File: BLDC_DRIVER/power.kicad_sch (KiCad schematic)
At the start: 0 parts

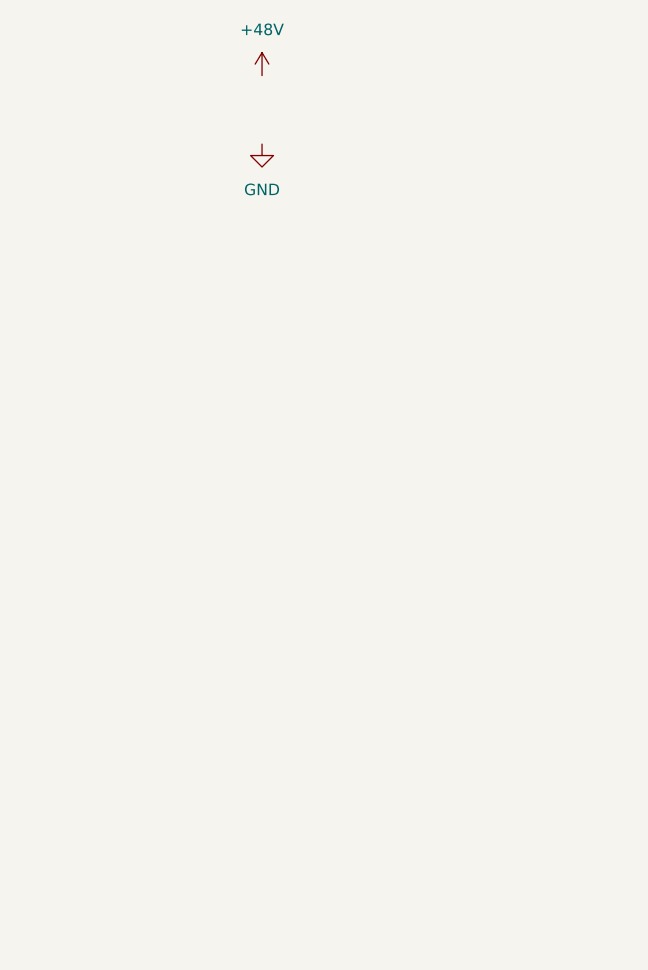
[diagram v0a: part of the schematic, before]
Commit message: buck and mcu added
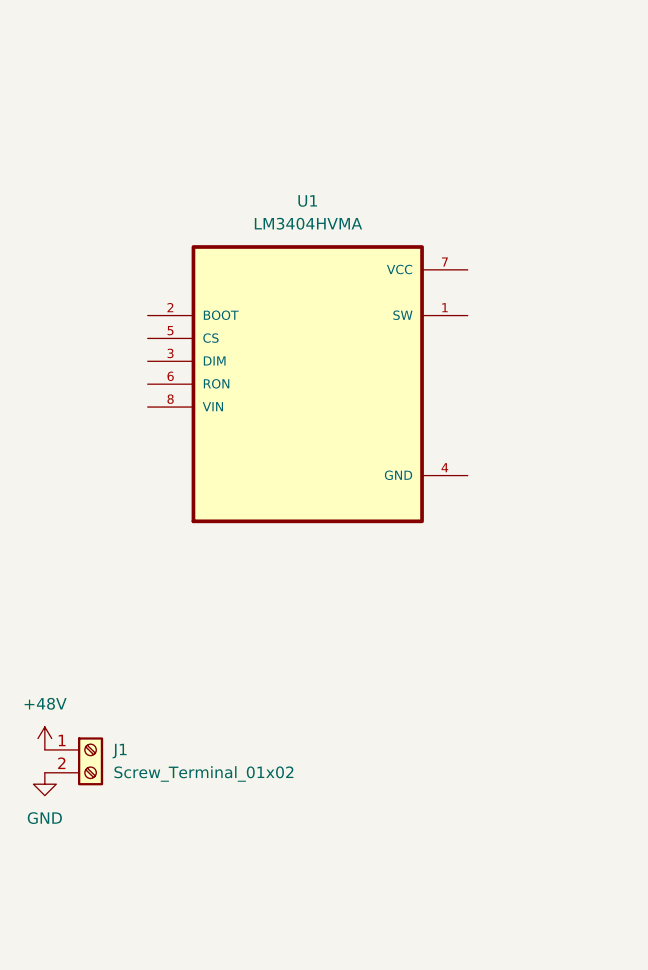
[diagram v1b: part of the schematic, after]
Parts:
- added J1: Screw_Terminal_01x02, TerminalBlock:TerminalBlock_MaiXu_MX126-5.0-02P_1x02_P5.00mm, symbol Connector:Screw_Terminal_01x02
- added U1: LM3404HVMA, LM3404:SOIC127P599X175-8N, symbol LM3404:LM3404HVMA
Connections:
- net +48V: now also J1.1 (Pin_1)
- net GND: now also J1.2 (Pin_2)

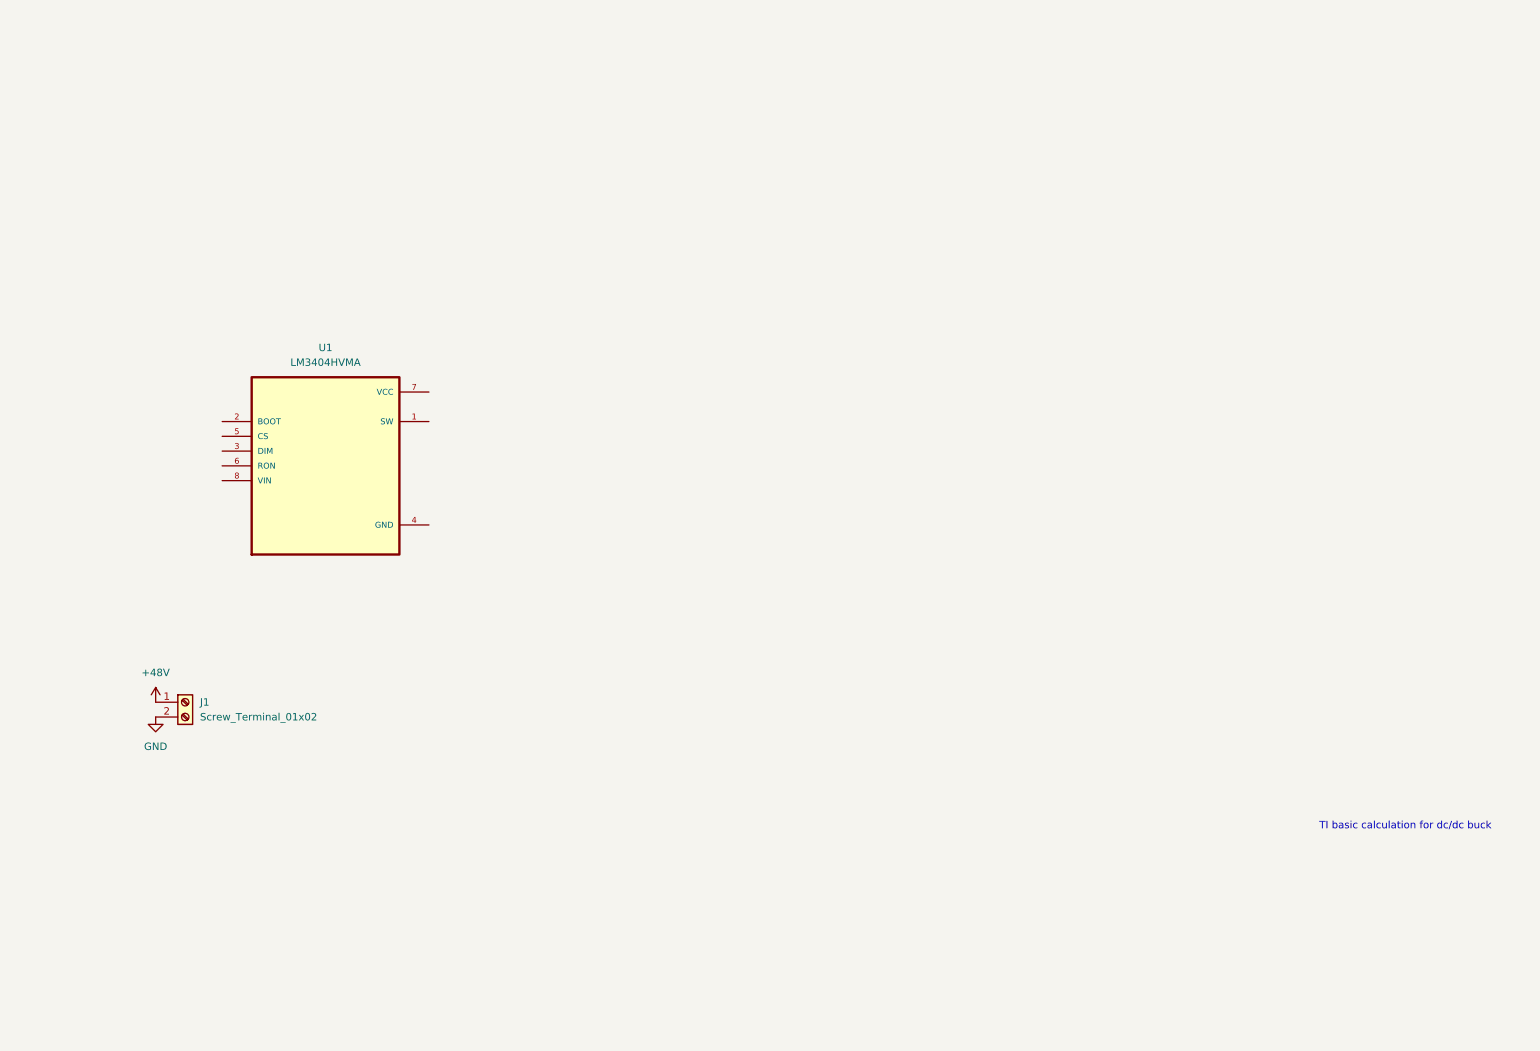
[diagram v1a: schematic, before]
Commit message: ldo added
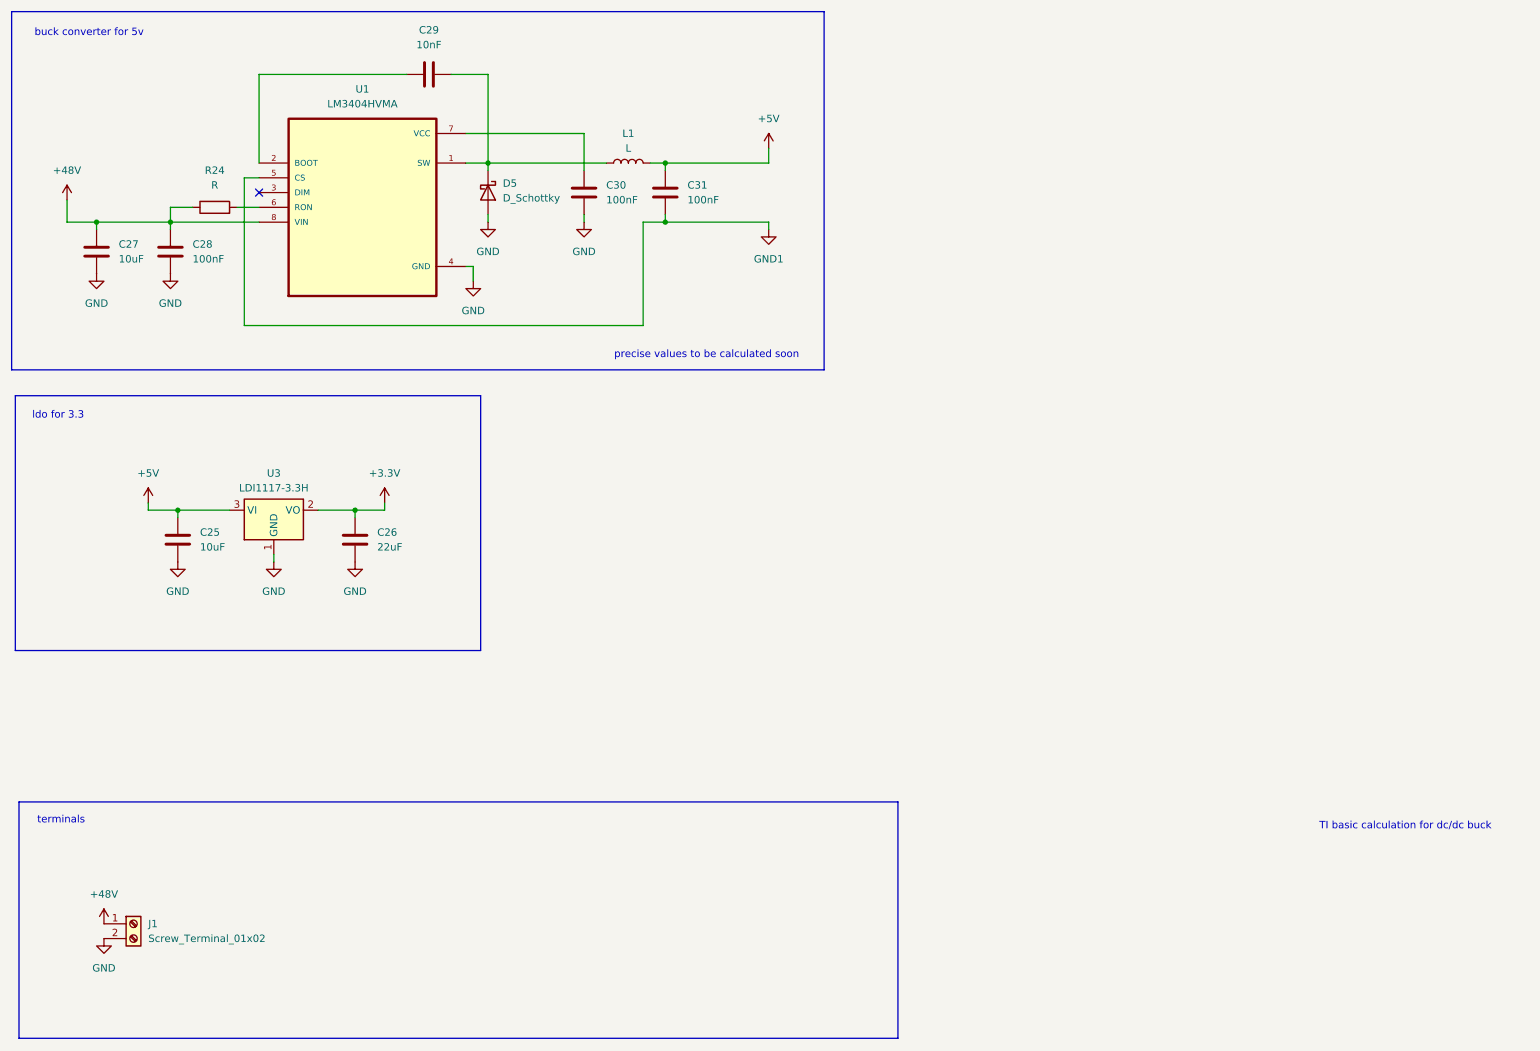
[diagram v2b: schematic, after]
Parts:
- added C25, C27: 10uF, symbol Device:C
- added C26: 22uF, symbol Device:C
- added C28, C30, C31: 100nF, symbol Device:C
- added C29: 10nF, symbol Device:C
- added D5: D_Schottky, symbol Device:D_Schottky
- added L1: L, symbol Device:L
- added R24: R, symbol Device:R
- added U3: LDI1117-3.3H, Package_TO_SOT_SMD:SOT-223-3_TabPin2, symbol Regulator_Linear:LM1117MP-3.3
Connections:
- net +48V: now also U1.8 (VIN), C27.1, C28.2, R24.1
- net GND: now also U1.4 (GND), C25.2, C26.2, C27.2, C28.1, C30.2, D5.2 (A), U3.1 (GND)
- net at U1.1 (SW): now also C29.2, D5.1 (K), L1.1
- net at U1.2 (BOOT): now also C29.1
- net GND1: now reaches U1.5 (CS)
- net GND1: now also C31.1
- net at U1.6 (RON): now also R24.2
- net at U1.7 (VCC): now also C30.1
- new net +3.3V: C26.1, U3.2 (VO)
- new net +5V: C25.1, C31.2, L1.2, U3.3 (VI)
- no-connect marks 0 -> 1
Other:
- note added: "buck converter for 5v"
- note added: "ldo for 3.3"
- note added: "precise values to be calculated soon"
- note added: "terminals"
- moved on the sheet: J1, U1

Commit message: mcu added
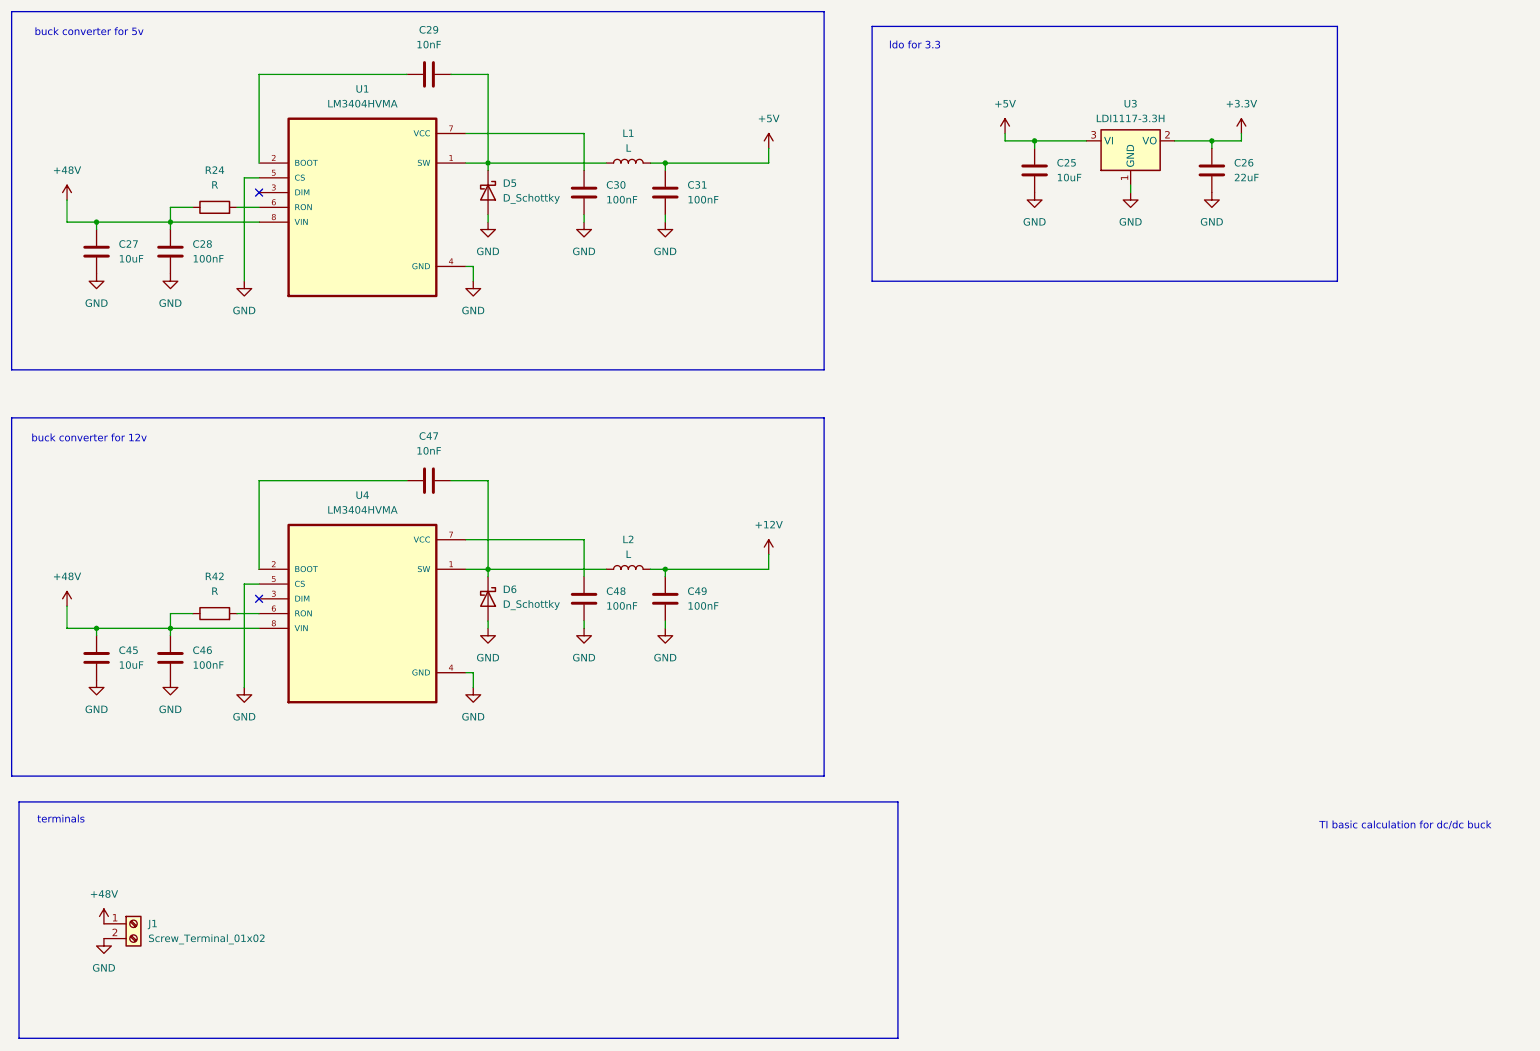
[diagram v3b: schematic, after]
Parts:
- added C45: 10uF, symbol Device:C
- added C46, C48, C49: 100nF, symbol Device:C
- added C47: 10nF, symbol Device:C
- added D6: D_Schottky, symbol Device:D_Schottky
- added L2: L, symbol Device:L
- added R42: R, symbol Device:R
- added U4: LM3404HVMA, LM3404:SOIC127P599X175-8N, symbol LM3404:LM3404HVMA
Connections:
- net GND1 is gone; now on net GND: C31.1, U1.5 (CS)
- net +48V: now also C45.1, C46.2, R42.1, U4.8 (VIN)
- net GND: now also C45.2, C46.1, C48.2, C49.1, D6.2 (A), U4.4 (GND), U4.5 (CS)
- new net: C47.1, U4.2 (BOOT)
- new net: C47.2, D6.1 (K), L2.1, U4.1 (SW)
- new net: C48.1, U4.7 (VCC)
- new net: R42.2, U4.6 (RON)
- new net +12V: C49.2, L2.2
- no-connect marks 1 -> 2
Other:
- note added: "buck converter for 12v"
- note removed: "precise values to be calculated soon"
- moved on the sheet: C25, C26, U3

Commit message: footprints added, cap values corrected
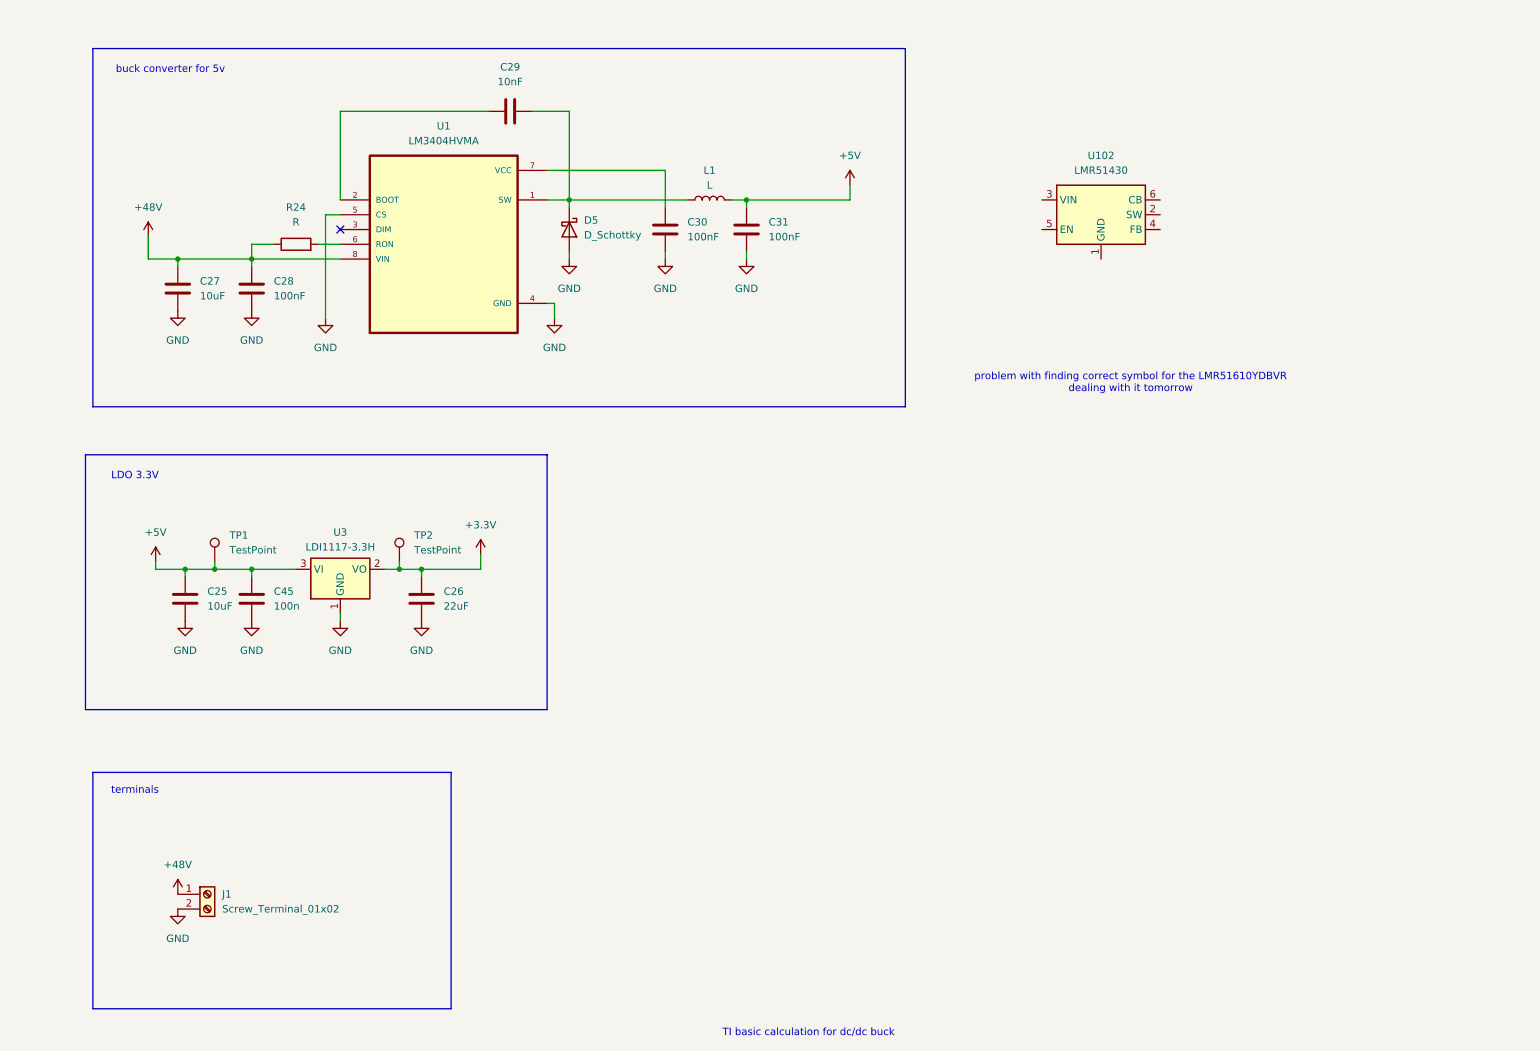
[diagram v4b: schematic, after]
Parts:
- removed C46, C48, C49: 100nF, symbol Device:C
- removed C47: 10nF, symbol Device:C
- removed D6: D_Schottky, symbol Device:D_Schottky
- removed L2: L, symbol Device:L
- removed R42: R, symbol Device:R
- removed U4: LM3404HVMA, LM3404:SOIC127P599X175-8N, symbol LM3404:LM3404HVMA
- added TP1, TP2: TestPoint, TestPoint:TestPoint_Pad_D1.5mm, symbol Connector:TestPoint
- added U102: LMR51430, Package_TO_SOT_SMD:SOT-23-6, symbol Regulator_Switching:LMR51430
- C45: value 10uF -> 100n
- J1: footprint TerminalBlock:TerminalBlock_MaiXu_MX126-5.0-02P_1x02_P5.00mm -> Connector_AMASS:AMASS_XT60-F_1x02_P7.20mm_Vertical
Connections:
- net +3.3V: now also TP2.1
- net +48V: no longer C45.1
- net +5V: now also C45.1, TP1.1
- no-connect marks 2 -> 1
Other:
- note added: "LDO 3.3V"
- note added: "problem with finding correct symbol for the LMR51610YDBVR dealing with it tomorrow"
- note removed: "buck converter for 12v"
- note removed: "ldo for 3.3"
- moved on the sheet: C25, C26, C27, C28, C29, C30, C31, D5, J1, L1, R24, U1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
